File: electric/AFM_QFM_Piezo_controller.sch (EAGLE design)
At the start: 41 parts, among them U1 LTC3260EMSE#PBF, U2 AD5696RARUZ-RL7RU_16_ADI-M, U3 LM324KAD

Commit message: allboards
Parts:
- added C10, C12, C8: 10uF, SparkFun-Capacitors:10UF-0805-10V-10%
- added C11, C13, C9: 0.1uF, eagle-ltspice:C
- added J2: (no value), SparkFun-Connectors:CONN_04LONGPADS
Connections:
- net N$10 renamed VOUTB
- net N$14 renamed SDA
- net N$15 renamed SCL
- net N$17 renamed VOUTA
- net N$20 renamed VOUTC
- net N$23 renamed V_REF
- net N$28 renamed VOUTD
- net N$31 renamed LDAC
- removed net GROUND: C7.2, R20.1, R4.1, U2.GND
- removed net N$11: C6.1, R3.2, U1.LDO-, U3.VCC-
- removed net N$13: C7.1, R14.2, R2.2, U1.LDO+, U2.!RESET, U2.RSTSEL, U2.VDD, U2.VLOGIC, U3.VCC+
- removed net N$26: R18.2, U3.OUT1
- removed net N$27: R17.2, U3.OUT2
- removed net N$29: R16.2, U3.OUT3
- removed net N$30: R19.2, U3.OUT4
- removed net N$5: C2.2, J1.2, U1.EN+, U1.EN-, U1.VIN
- new net LDO+: C7.1, C8.1, C9.1, R14.2, R2.2, U1.LDO+, U3.VCC+
- new net LDO-: C10.1, C11.1, C6.1, R3.2, U1.LDO-, U3.VCC-
- new net P_OUT1: J2.1, R18.2, U3.OUT1
- new net P_OUT2: J2.2, R17.2, U3.OUT2
- new net P_OUT3: J2.3, R16.2, U3.OUT3
- new net P_OUT4: J2.4, R19.2, U3.OUT4
- new net VDD: C12.1, C13.1, C2.2, J1.2, R20.1, U1.EN+, U1.EN-, U1.VIN, U2.!RESET, U2.GAIN, U2.RSTSEL, U2.VDD, U2.VLOGIC
- net AGND: now also B1.GND@0, B1.GND@1, B1.GND@2, C10.2, C11.2, C12.2, C13.2, C7.2, C8.2, C9.2, J1.1, R4.1, U2.GND; no longer J1.3, U2.GAIN
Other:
- moved on the sheet: J1

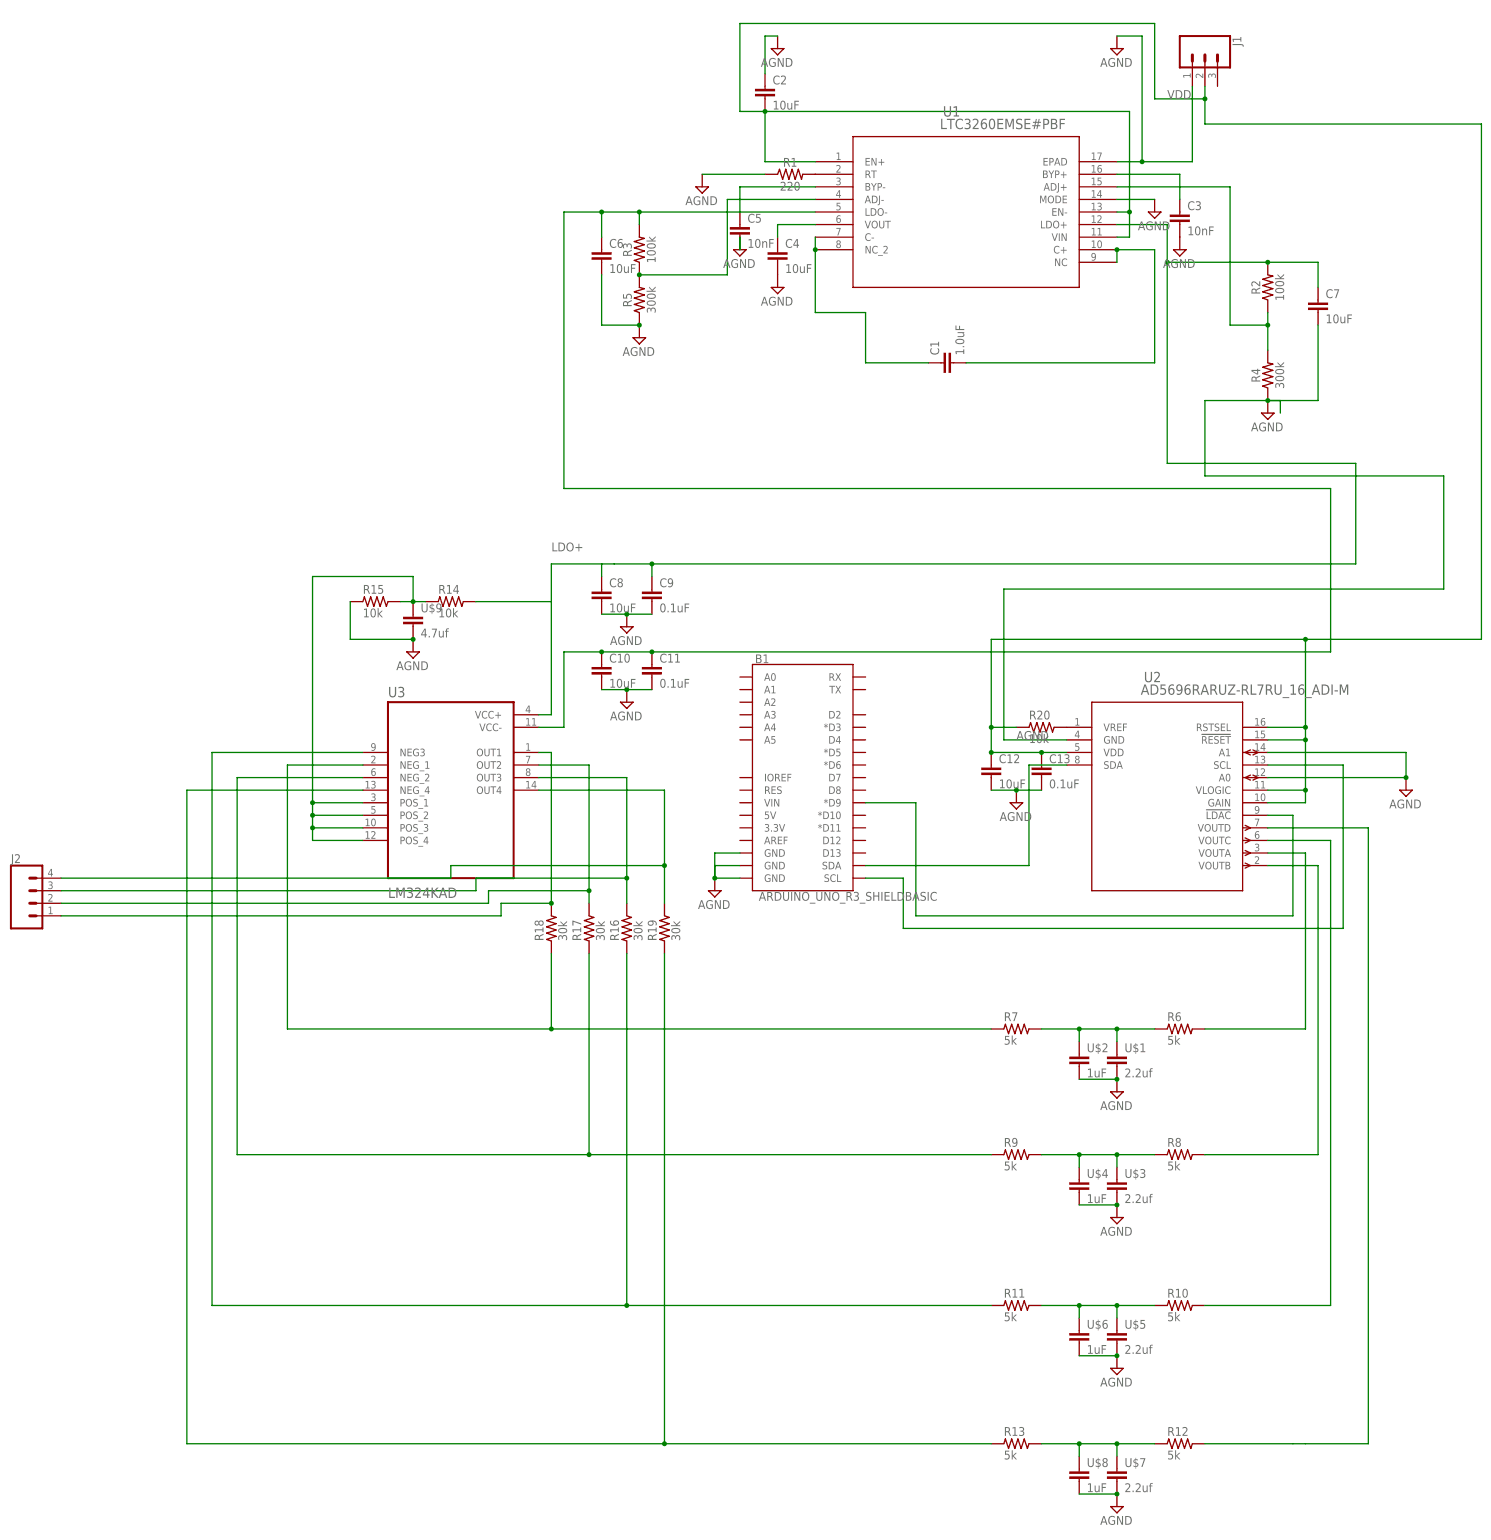
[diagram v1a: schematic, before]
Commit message: Charge pump with his own power source
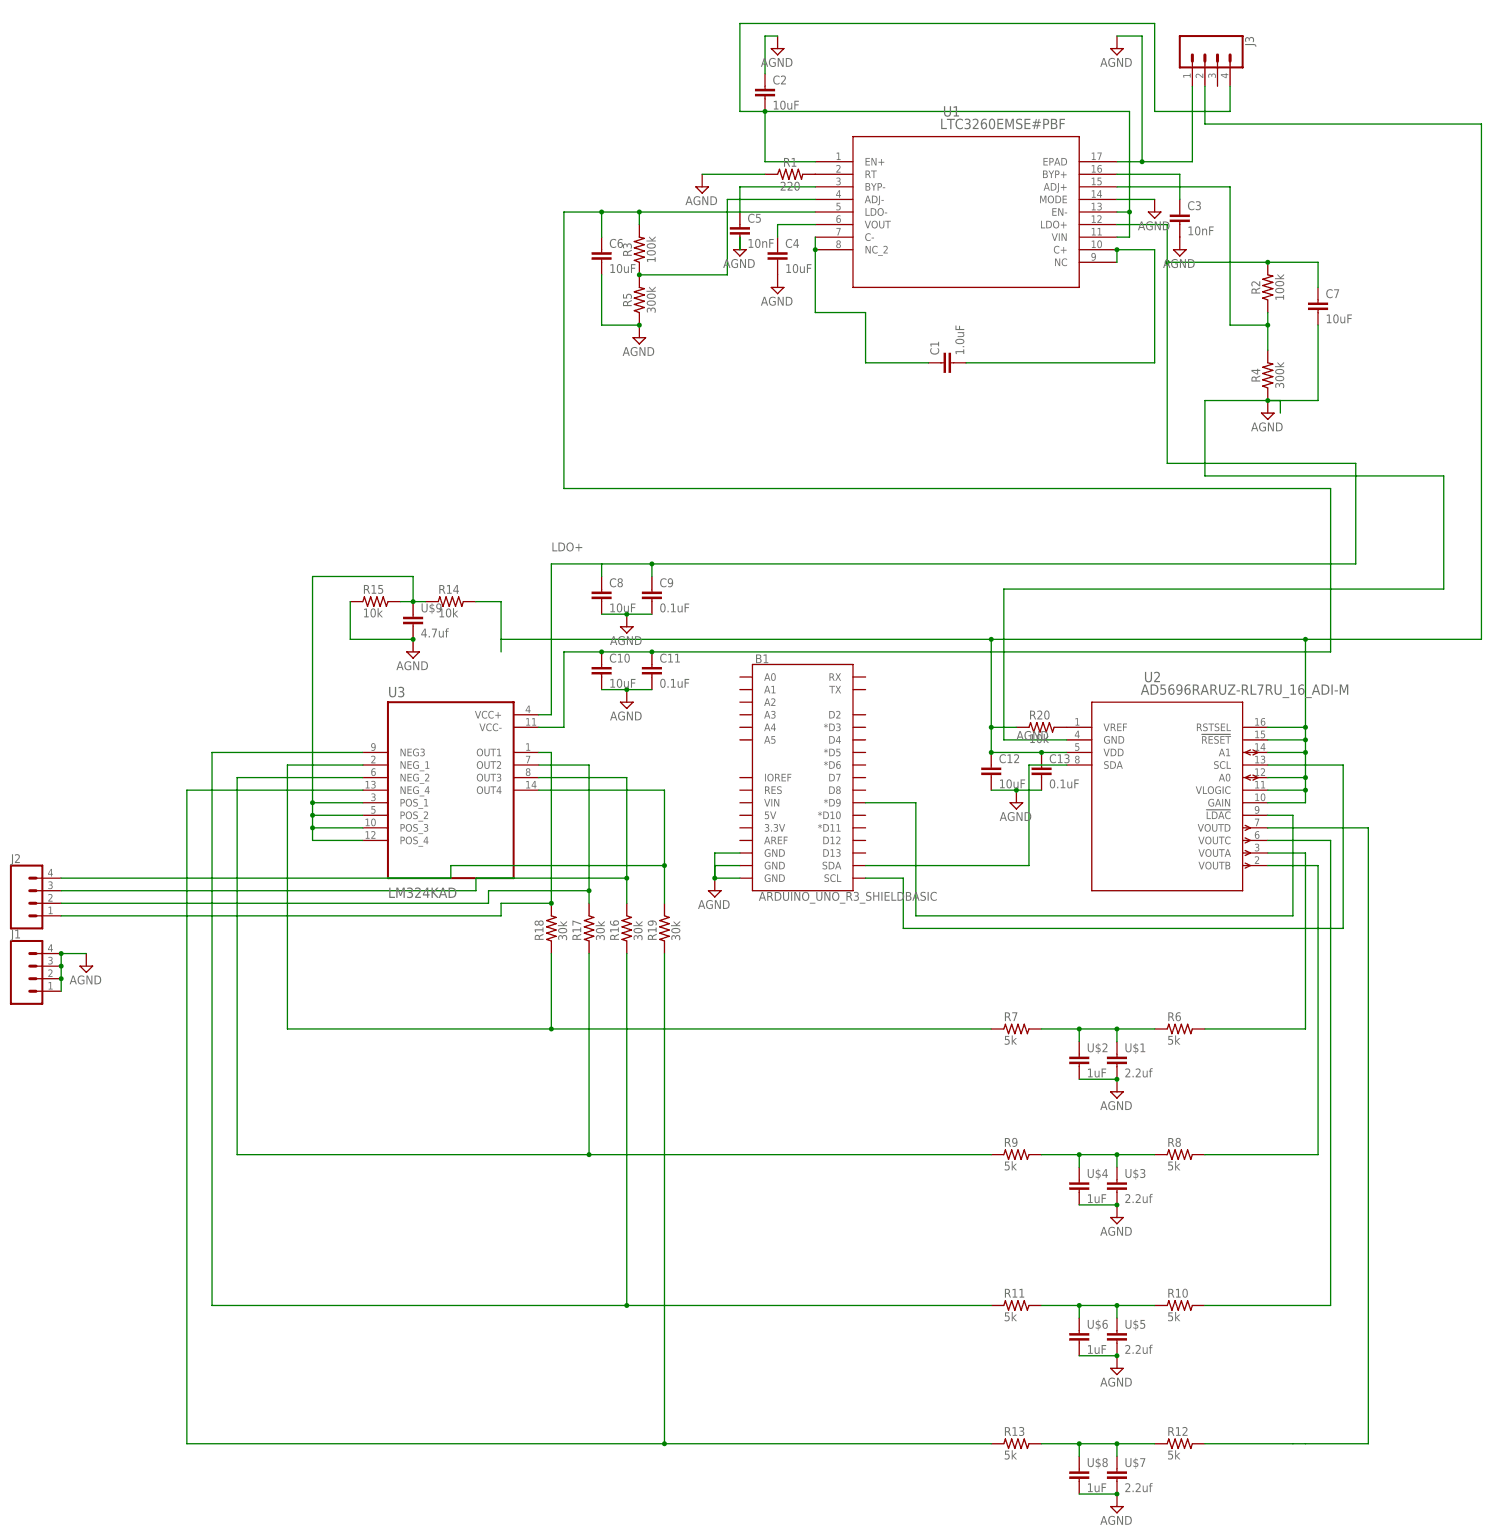
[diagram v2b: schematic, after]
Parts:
- added J3: (no value), SparkFun-Connectors:CONN_04LONGPADS
- J1: device SparkFun-Connectors:CONN_03LONGPADS -> SparkFun-Connectors:CONN_04LONGPADS
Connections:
- new net V15+: C2.2, J3.4, U1.EN+, U1.EN-, U1.VIN
- net AGND: now also J1.2, J1.3, J1.4, J3.1; no longer U2.A0, U2.A1
- net LDO+: no longer R14.2
- net VDD: now also J3.2, R14.2, U2.A0, U2.A1; no longer C2.2, J1.2, U1.EN+, U1.EN-, U1.VIN

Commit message: newer electroincs
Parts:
- J1: device SparkFun-Connectors:CONN_04LONGPADS -> SparkFun-Connectors:CONN_01PTH_LONGPAD
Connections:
- net AGND: no longer J1.2, J1.3, J1.4
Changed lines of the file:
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@@
 <part name="SUPPLY19" library="Power_Symbols" library_urn="urn:adsk.eagle:library:16502351" deviceset="AGND" device="" value="AGND"/>
 <part name="J3" library="SparkFun-Connectors" library_urn="urn:adsk.eagle:library:513" deviceset="CONN_04" device="LONGPADS" package3d_urn="urn:adsk.eagle:package:38098/2"/>
-<part name="J1" library="SparkFun-Connectors" library_urn="urn:adsk.eagle:library:513" deviceset="CONN_04" device="LONGPADS" package3d_urn="urn:adsk.eagle:package:38098/2"/>
 <part name="SUPPLY15" library="Power_Symbols" library_urn="urn:adsk.eagle:library:16502351" deviceset="AGND" device="" value="AGND"/>
+<part name="J1" library="SparkFun-Connectors" library_urn="urn:adsk.eagle:library:513" deviceset="CONN_01" device="PTH_LONGPAD" package3d_urn="urn:adsk.eagle:package:38030/2"/>
 </parts>
 <sheets>
@@
 <attribute name="NAME" x="107.188" y="119.38" size="1.778" layer="95" font="vector" rot="R270"/>
 </instance>
-<instance part="J1" gate="J1" x="-137.16" y="-71.12" smashed="yes">
-<attribute name="VALUE" x="-142.24" y="-78.486" size="1.778" layer="96" font="vector"/>
-<attribute name="NAME" x="-142.24" y="-62.992" size="1.778" layer="95" font="vector"/>
-</instance>
 <instance part="SUPPLY15" gate="G$1" x="-127" y="-68.58" smashed="yes">
 <attribute name="VALUE" x="-127.127" y="-72.263" size="1.778" layer="96" align="bottom-center"/>
+</instance>
+<instance part="J1" gate="J1" x="-139.7" y="-66.04" smashed="yes">
+<attribute name="VALUE" x="-142.24" y="-70.866" size="1.778" layer="96" font="vector"/>
+<attribute name="NAME" x="-142.24" y="-62.992" size="1.778" layer="95" font="vector"/>
 </instance>
 </instances>
@@
 </segment>
 <segment>
-<pinref part="J1" gate="J1" pin="4"/>
 <pinref part="SUPPLY15" gate="G$1" pin="AGND"/>
 <wire x1="-132.08" y1="-66.04" x2="-127" y2="-66.04" width="0.1524" layer="91"/>
-<pinref part="J1" gate="J1" pin="3"/>
-<wire x1="-132.08" y1="-68.58" x2="-132.08" y2="-66.04" width="0.1524" layer="91"/>
+<wire x1="-132.08" y1="-73.66" x2="-132.08" y2="-66.04" width="0.1524" layer="91"/>
+<pinref part="J1" gate="J1" pin="1"/>
 <junction x="-132.08" y="-66.04"/>
-<pinref part="J1" gate="J1" pin="2"/>
-<wire x1="-132.08" y1="-71.12" x2="-132.08" y2="-68.58" width="0.1524" layer="91"/>
-<junction x="-132.08" y="-68.58"/>
-<pinref part="J1" gate="J1" pin="1"/>
-<wire x1="-132.08" y1="-73.66" x2="-132.08" y2="-71.12" width="0.1524" layer="91"/>
-<junction x="-132.08" y="-71.12"/>
 </segment>
 </net>
